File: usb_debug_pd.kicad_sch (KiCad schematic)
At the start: 84 parts, among them J4 Tag-Connect_TC2050-IDC-NL_2x5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, J7 USB-C_GCT_USB4105-GF-A, Q12 PJE138K, Q3 PJE138K, U29 W25Q80DV_USON, U30 TPS65988DHRSHR, U31 NTS0102_XSON, U32 NCP730BMT330_WSON, U34 FT230X_QFN, U40 AP22615A_TSOT26, U42 TPD4E05U06QDQARQ1

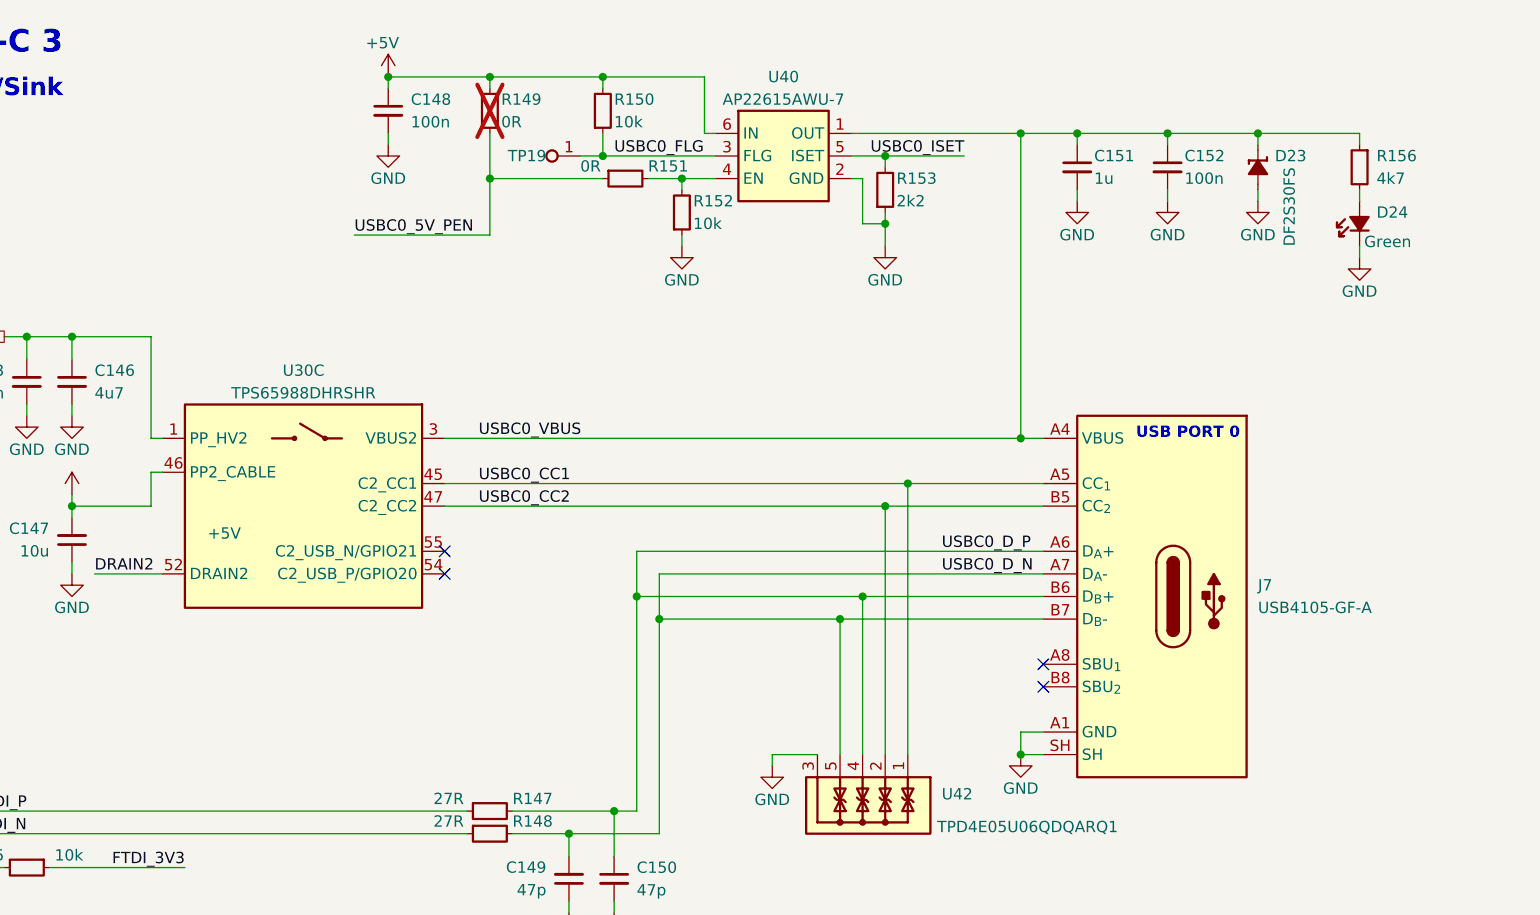
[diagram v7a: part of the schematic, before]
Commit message: [#83224] Place USB Debug section
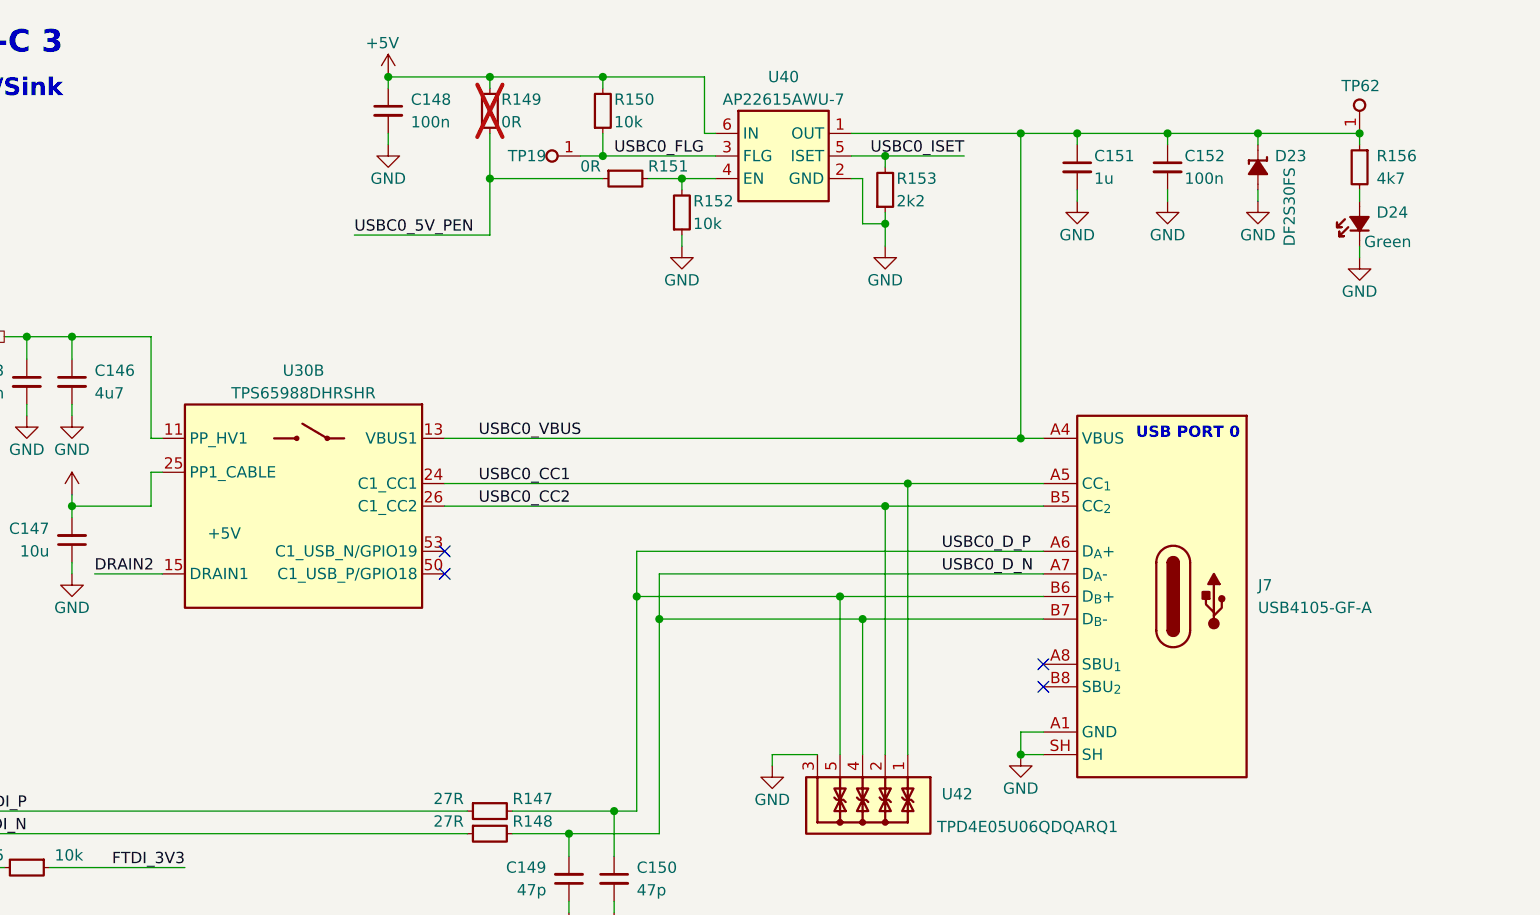
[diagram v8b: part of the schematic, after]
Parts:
- added TP62: TP_0.75mm_SMD, antmicro-footprints:TP_SMD_0.75mm, symbol antmicroTestPoints:TP_0.75mm_SMD
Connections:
- net +5V: now also U30.25 (PP1_CABLE); no longer U30.46 (PP2_CABLE)
- net DRAIN2: now also U30.15 (DRAIN1), U30.19 (DRAIN1), U30.58 (DRAIN1), U30.8 (DRAIN1); no longer U30.52 (DRAIN2), U30.56 (DRAIN2), U30.57 (DRAIN2), U30.7 (DRAIN2)
- net USBC0_CC1: now also U30.24 (C1_CC1); no longer U30.45 (C2_CC1)
- net USBC0_CC2: now also U30.26 (C1_CC2); no longer U30.47 (C2_CC2)
- net USBC0_D_N: now also U42.4, U42.7; no longer U42.5, U42.6
- net USBC0_D_P: now also U42.5, U42.6; no longer U42.4, U42.7
- net USBC0_VBUS: now also U30.13 (VBUS1), TP62.1; no longer U30.3 (VBUS2)
- net USBPD2_HV: now also U30.11 (PP_HV1); no longer U30.1 (PP_HV2)
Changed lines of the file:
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@@
 	)
 	(junction
-		(at 300.99 86.36)
-		(diameter 0)
-		(color 0 0 0 0)
-	)
-	(junction
 		(at 328.93 210.82)
 		(diameter 0)
@@
 	)
 	(junction
+		(at 359.41 31.75)
+		(diameter 0)
+		(color 0 0 0 0)
+	)
+	(junction
 		(at 306.07 73.66)
 		(diameter 0)
@@
 	)
 	(junction
-		(at 303.53 83.82)
+		(at 261.62 25.4)
 		(diameter 0)
 		(color 0 0 0 0)
 	)
 	(junction
-		(at 261.62 25.4)
+		(at 300.99 83.82)
 		(diameter 0)
 		(color 0 0 0 0)
@@
 	)
 	(junction
+		(at 303.53 86.36)
+		(diameter 0)
+		(color 0 0 0 0)
+	)
+	(junction
 		(at 91.44 64.77)
 		(diameter 0)
@@
 	(wire
 		(pts
-			(xy 303.53 83.82) (xy 303.53 101.6)
+			(xy 300.99 83.82) (xy 300.99 101.6)
 		)
 		(stroke
@@
 	(wire
 		(pts
+			(xy 303.53 86.36) (xy 323.85 86.36)
+		)
+		(stroke
+			(width 0)
+			(type default)
+		)
+	)
+	(wire
+		(pts
 			(xy 321.31 31.75) (xy 321.31 66.04)
 		)
@@
 	(wire
 		(pts
-			(xy 300.99 86.36) (xy 323.85 86.36)
-		)
-		(stroke
-			(width 0)
-			(type default)
-		)
-	)
-	(wire
-		(pts
 			(xy 247.65 231.14) (xy 255.27 231.14)
 		)
@@
 	(wire
 		(pts
-			(xy 97.79 120.65) (xy 97.79 121.92)
+			(xy 300.99 83.82) (xy 323.85 83.82)
 		)
 		(stroke
@@
 	(wire
 		(pts
-			(xy 180.34 193.04) (xy 180.34 185.42)
+			(xy 97.79 120.65) (xy 97.79 121.92)
 		)
 		(stroke
@@
 	(wire
 		(pts
-			(xy 86.36 203.2) (xy 91.44 203.2)
+			(xy 180.34 193.04) (xy 180.34 185.42)
 		)
 		(stroke
@@
 	(wire
 		(pts
-			(xy 138.43 196.85) (xy 138.43 198.12)
+			(xy 86.36 203.2) (xy 91.44 203.2)
 		)
 		(stroke
@@
 	(wire
 		(pts
-			(xy 242.57 227.33) (xy 242.57 257.81)
+			(xy 138.43 196.85) (xy 138.43 198.12)
 		)
 		(stroke
@@
 	(wire
 		(pts
-			(xy 303.53 83.82) (xy 323.85 83.82)
+			(xy 242.57 227.33) (xy 242.57 257.81)
 		)
 		(stroke
@@
 	(wire
 		(pts
-			(xy 280.67 86.36) (xy 300.99 86.36)
+			(xy 280.67 86.36) (xy 303.53 86.36)
 		)
 		(stroke
@@
 	(wire
 		(pts
-			(xy 300.99 86.36) (xy 300.99 101.6)
+			(xy 303.53 86.36) (xy 303.53 101.6)
 		)
 		(stroke
@@
 	(wire
 		(pts
-			(xy 278.13 83.82) (xy 303.53 83.82)
+			(xy 278.13 83.82) (xy 300.99 83.82)
 		)
 		(stroke
@@
 		(at 256.54 66.04 0)
 		(mirror y)
-		(unit 3)
+		(unit 2)
 		(exclude_from_sim no)
 		(in_bom yes)
@@
 				(path "/f569b0be-0afd-48b7-93ee-28582a4c645c/12c19ba5-8fdc-4775-a33b-e8b1ade01b0a"
 					(reference "U30")
-					(unit 3)
+					(unit 2)
 				)
 			)
@@
 					(unit 1)
 				)
+			)
+		)
+	)
+	(symbol
+		(lib_name "TP_0.75mm_SMD_10")
+		(lib_id "antmicroTestPoints:TP_0.75mm_SMD")
+		(at 359.41 31.75 90)
+		(unit 1)
+		(exclude_from_sim no)
+		(in_bom no)
+		(on_board yes)
+		(dnp no)
+		(property "Reference" "TP62"
+			(at 361.696 26.416 90)
+			(effects
+				(font
+					(size 1.27 1.27)
+				)
+				(justify left)
+			)
+		)
+		(property "Value" "TP_0.75mm_SMD"
+			(at 363.22 21.59 0)
+			(effects
+				(font
+					(size 1.27 1.27)
+					(thickness 0.15)
+				)
+				(justify left bottom)
+				(hide yes)
+			)
+		)
+		(property "Footprint" "antmicro-footprints:TP_SMD_0.75mm"
+			(at 365.76 21.59 0)
+			(effects
+				(font
+					(size 1.27 1.27)
+					(thickness 0.15)
+				)
+				(justify left bottom)
+				(hide yes)
+			)
+		)
+		(property "Datasheet" ""
+			(at 372.11 13.97 0)
+			(effects
+				(font
+					(size 1.27 1.27)
+					(thickness 0.15)
+				)
+				(justify left bottom)
+				(hide yes)
+			)
+		)
+		(property "Description" ""
+			(at 359.41 31.75 0)
+			(effects
+				(font
+					(size 1.27 1.27)
+				)
+				(hide yes)
+			)
+		)
+		(property "MPN" ""
+			(at 370.84 20.955 0)
+			(effects
+				(font
+					(size 1.27 1.27)
+					(thickness 0.15)
+				)
+				(justify left bottom)
+				(hide yes)
+			)
+		)
+		(property "Manufacturer" ""
+			(at 365.76 20.955 0)
+			(effects
+				(font
+					(size 1.27 1.27)
+					(thickness 0.15)
+				)
+				(justify left bottom)
+				(hide yes)
+			)
+		)
+		(property "Author" "Antmicro"
+			(at 368.3 21.59 0)
+			(effects
+				(font
+					(size 1.27 1.27)
+					(thickness 0.15)
+				)
+				(justify left bottom)
+				(hide yes)
+			)
+		)
+		(property "License" "Apache-2.0"
+			(at 370.84 21.59 0)
+			(effects
+				(font
+					(size 1.27 1.27)
+					(thickness 0.15)
+				)
+				(justify left bottom)
+				(hide yes)
+			)
+		)
+		(pin "1"
+		)
+		(instances
+			(project "jetson-agx-thor-baseboard"
+				(path "/f569b0be-0afd-48b7-93ee-28582a4c645c/12c19ba5-8fdc-4775-a33b-e8b1ade01b0a"
+					(reference "TP62")
+					(unit 1)
+				)
